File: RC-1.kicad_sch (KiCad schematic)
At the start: 0 parts

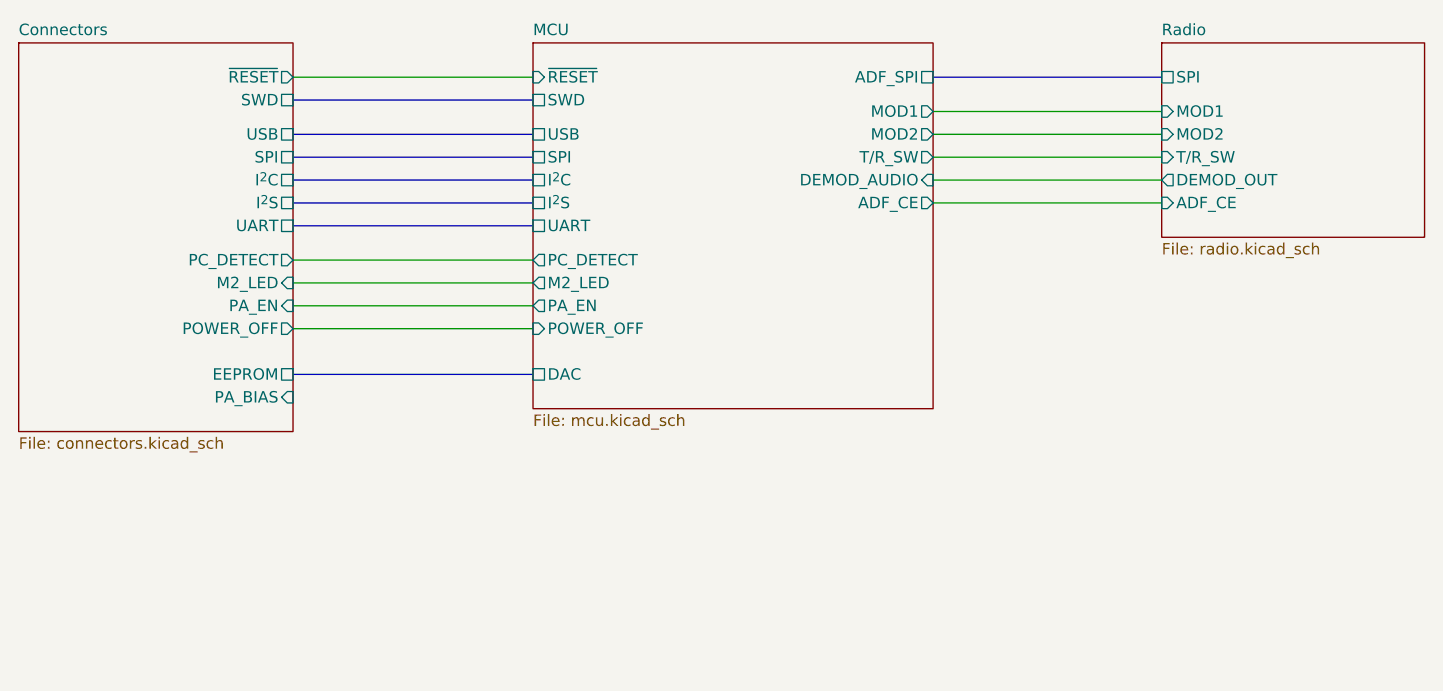
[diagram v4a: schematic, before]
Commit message: Set up ADF7021 for single RF output, 2-point modulation
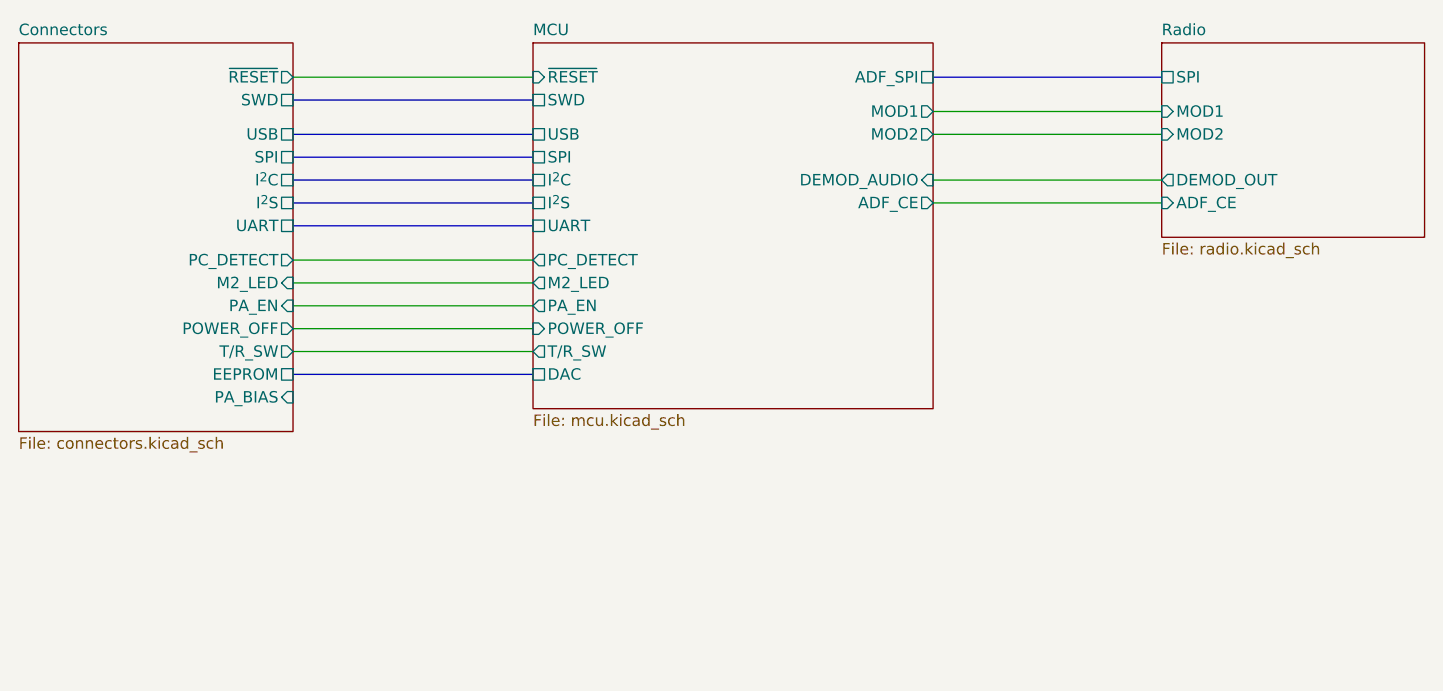
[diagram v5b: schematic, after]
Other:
- sheet Connectors ports: added T/R_SW; removed none
- sheet Radio ports: added none; removed T/R_SW
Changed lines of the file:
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@@
     (stroke (width 0) (type default) (color 0 0 0 0))
   )
-  (wire (pts (xy 175.26 93.98) (xy 200.66 93.98))
+  (wire (pts (xy 130.81 115.57) (xy 104.14 115.57))
     (stroke (width 0) (type default) (color 0 0 0 0))
   )
@@
       (effects (font (size 1.27 1.27)) (justify right))
     )
-    (pin "T{slash}R_SW" output (at 175.26 93.98 0)
-      (effects (font (size 1.27 1.27)) (justify right))
+    (pin "T{slash}R_SW" output (at 130.81 115.57 180)
+      (effects (font (size 1.27 1.27)) (justify left))
     )
     (pin "DEMOD_AUDIO" input (at 175.26 96.52 0)
@@
       (effects (font (size 1.27 1.27)) (justify right))
     )
+    (pin "T{slash}R_SW" output (at 104.14 115.57 0)
+      (effects (font (size 1.27 1.27)) (justify right))
+    )
   )
   (sheet (at 200.66 81.28) (size 29.21 21.59) (fields_autoplaced)
@@
       (effects (font (size 1.27 1.27)) (justify left top))
     )
-    (pin "T{slash}R_SW" input (at 200.66 93.98 180)
-      (effects (font (size 1.27 1.27)) (justify left))
-    )
     (pin "MOD2" input (at 200.66 91.44 180)
       (effects (font (size 1.27 1.27)) (justify left))
@@
       (reference "#PWR?") (unit 1) (value "+3V3") (footprint "")
     )
+    (path "/e9b5eb9e-a5da-44ea-89cf-1dbc5f8707b1/1950a0c7-f402-4b5c-a508-849658a6f4d3"
+      (reference "#PWR?") (unit 1) (value "GND") (footprint "")
+    )
     (path "/e9b5eb9e-a5da-44ea-89cf-1dbc5f8707b1/1b350a9d-a408-4dfa-a32b-dc704a4a856d"
       (reference "#PWR?") (unit 1) (value "GND") (footprint "")
@@
       (reference "#PWR?") (unit 1) (value "GND") (footprint "")
     )
+    (path "/e9b5eb9e-a5da-44ea-89cf-1dbc5f8707b1/2c4a4823-3df4-4715-82e4-ace04f59e52b"
+      (reference "#PWR?") (unit 1) (value "GND") (footprint "")
+    )
     (path "/e9b5eb9e-a5da-44ea-89cf-1dbc5f8707b1/321442de-1be8-447c-864f-6a257a7c6538"
       (reference "#PWR?") (unit 1) (value "GND") (footprint "")
@@
     )
     (path "/e9b5eb9e-a5da-44ea-89cf-1dbc5f8707b1/48b252b8-2440-494d-9928-f82258d5af1c"
+      (reference "#PWR?") (unit 1) (value "GND") (footprint "")
+    )
+    (path "/e9b5eb9e-a5da-44ea-89cf-1dbc5f8707b1/4d8c1cd9-f911-4b73-9309-ada4c43200a2"
       (reference "#PWR?") (unit 1) (value "GND") (footprint "")
     )
@@
       (reference "#PWR?") (unit 1) (value "GND") (footprint "")
     )
+    (path "/e9b5eb9e-a5da-44ea-89cf-1dbc5f8707b1/56056a77-a219-4861-a216-23f1af2f53ef"
+      (reference "#PWR?") (unit 1) (value "+3V3") (footprint "")
+    )
     (path "/37f64190-0af6-4571-a391-bfca4fb830ce/5a9912a7-bc78-4975-becd-a93d7e6ca124"
       (reference "#PWR?") (unit 1) (value "+3V3") (footprint "")
@@
     )
     (path "/e9b5eb9e-a5da-44ea-89cf-1dbc5f8707b1/857e3f02-6033-4b41-84a2-b44b517994ba"
+      (reference "#PWR?") (unit 1) (value "GND") (footprint "")
+    )
+    (path "/e9b5eb9e-a5da-44ea-89cf-1dbc5f8707b1/88e64f20-39b1-43e3-bc15-63ee762477d0"
       (reference "#PWR?") (unit 1) (value "GND") (footprint "")
     )
@@
       (reference "#PWR?") (unit 1) (value "+3V3") (footprint "")
     )
+    (path "/e9b5eb9e-a5da-44ea-89cf-1dbc5f8707b1/b49bf0fd-c72b-4a40-94e9-b96d52cc906a"
+      (reference "#PWR?") (unit 1) (value "GND") (footprint "")
+    )
     (path "/37f64190-0af6-4571-a391-bfca4fb830ce/be7cb700-3d99-4cd8-9ce6-aeefb1daeab8"
       (reference "#PWR?") (unit 1) (value "+3V3") (footprint "")
@@
       (reference "#PWR?") (unit 1) (value "+3V3") (footprint "")
     )
+    (path "/e9b5eb9e-a5da-44ea-89cf-1dbc5f8707b1/d0db605f-f64d-4084-99f0-1f083aec5dda"
+      (reference "#PWR?") (unit 1) (value "GND") (footprint "")
+    )
     (path "/d054b6a0-3a84-4aaa-901c-78f33fd51c3e/d8415da7-949b-463f-944b-f60c21219035"
       (reference "#PWR?") (unit 1) (value "GND") (footprint "")
@@
     (path "/37f64190-0af6-4571-a391-bfca4fb830ce/fa5153d6-bd2e-481c-acf5-a582605af947"
       (reference "#PWR?") (unit 1) (value "GND") (footprint "")
+    )
+    (path "/e9b5eb9e-a5da-44ea-89cf-1dbc5f8707b1/0101861e-4de8-4162-b9fa-983060e95190"
+      (reference "C?") (unit 1) (value "6p8") (footprint "Capacitor_SMD:C_0402_1005Metric")
     )
     (path "/37f64190-0af6-4571-a391-bfca4fb830ce/018002e6-06ae-46c7-887f-c27f45825467"
@@
       (reference "C?") (unit 1) (value "100n") (footprint "Capacitor_SMD:C_0402_1005Metric")
     )
+    (path "/e9b5eb9e-a5da-44ea-89cf-1dbc5f8707b1/69082dc9-e612-439f-b4a5-50360abc5713"
+      (reference "C?") (unit 1) (value "1n5") (footprint "Capacitor_SMD:C_0603_1608Metric")
+    )
     (path "/e9b5eb9e-a5da-44ea-89cf-1dbc5f8707b1/6c002c11-1dba-4213-acac-eaa28178d048"
       (reference "C?") (unit 1) (value "6p8") (footprint "Capacitor_SMD:C_0402_1005Metric")
@@
       (reference "C?") (unit 1) (value "10n") (footprint "Capacitor_SMD:C_0402_1005Metric")
     )
+    (path "/e9b5eb9e-a5da-44ea-89cf-1dbc5f8707b1/777b7d5e-dac0-4871-a578-c644ad7014c7"
+      (reference "C?") (unit 1) (value "1n5") (footprint "Capacitor_SMD:C_0603_1608Metric")
+    )
+    (path "/e9b5eb9e-a5da-44ea-89cf-1dbc5f8707b1/92b7986c-f593-49ae-8d36-f50fcd9da6e2"
+      (reference "C?") (unit 1) (value "1n5") (footprint "Capacitor_SMD:C_0603_1608Metric")
+    )
+    (path "/e9b5eb9e-a5da-44ea-89cf-1dbc5f8707b1/a03ac130-fa79-40b1-a286-2b47aff1a3e5"
+      (reference "C?") (unit 1) (value "10n") (footprint "Capacitor_SMD:C_0402_1005Metric")
+    )
     (path "/37f64190-0af6-4571-a391-bfca4fb830ce/a3ee2e41-11fd-443f-86c5-416e10b6f0a0"
       (reference "C?") (unit 1) (value "100n") (footprint "Capacitor_SMD:C_0402_1005Metric")
@@
       (reference "C?") (unit 1) (value "100n") (footprint "Capacitor_SMD:C_0402_1005Metric")
     )
+    (path "/e9b5eb9e-a5da-44ea-89cf-1dbc5f8707b1/d4e5561e-4a4e-484b-ad69-8cb687deefc3"
+      (reference "C?") (unit 1) (value "220p") (footprint "Capacitor_SMD:C_0402_1005Metric")
+    )
     (path "/37f64190-0af6-4571-a391-bfca4fb830ce/dbc23c1d-f9c7-4c2e-b8da-96344fb20002"
       (reference "C?") (unit 1) (value "TBD") (footprint "Capacitor_SMD:C_0402_1005Metric")
@@
       (reference "J?") (unit 1) (value "U.FL") (footprint "Connector_Coaxial:U.FL_Hirose_U.FL-R-SMT-1_Vertical")
     )
+    (path "/e9b5eb9e-a5da-44ea-89cf-1dbc5f8707b1/428c4882-4fa2-4105-96dc-a3e7f24d9294"
+      (reference "L?") (unit 1) (value "20n") (footprint "Inductor_SMD:L_0603_1608Metric")
+    )
     (path "/e9b5eb9e-a5da-44ea-89cf-1dbc5f8707b1/8d7ae6cb-fe9e-418c-b7a9-b5bf2fb70c94"
       (reference "L?") (unit 1) (value "27n") (footprint "Inductor_SMD:L_0402_1005Metric")
     )
+    (path "/e9b5eb9e-a5da-44ea-89cf-1dbc5f8707b1/978703e1-c453-44f6-8424-3709a0ab4260"
+      (reference "L?") (unit 1) (value "22n") (footprint "Inductor_SMD:L_0603_1608Metric")
+    )
     (path "/37f64190-0af6-4571-a391-bfca4fb830ce/bdf5539d-1394-4ecb-ae85-1bb323c82721"
       (reference "L?") (unit 1) (value "10uH") (footprint "")
     )
+    (path "/e9b5eb9e-a5da-44ea-89cf-1dbc5f8707b1/d72d702d-497f-4bad-82eb-724930a27ad6"
+      (reference "L?") (unit 1) (value "13n") (footprint "Inductor_SMD:L_0402_1005Metric")
+    )
     (path "/e9b5eb9e-a5da-44ea-89cf-1dbc5f8707b1/e850d9e7-ba6d-4b13-88a3-4477f9540cd9"
       (reference "L?") (unit 1) (value "DNP") (footprint "Inductor_SMD:L_0603_1608Metric")
@@
       (reference "R?") (unit 1) (value "100k") (footprint "Resistor_SMD:R_0402_1005Metric")
     )
+    (path "/e9b5eb9e-a5da-44ea-89cf-1dbc5f8707b1/547c7d2e-dd6a-4751-bc89-ad162b03611c"
+      (reference "R?") (unit 1) (value "5k6") (footprint "Resistor_SMD:R_0603_1608Metric")
+    )
     (path "/37f64190-0af6-4571-a391-bfca4fb830ce/57824045-fda2-4d7c-9a10-82e8e242782c"
       (reference "R?") (unit 1) (value "4k7") (footprint "")
@@
       (reference "R?") (unit 1) (value "4k7") (footprint "")
     )
+    (path "/e9b5eb9e-a5da-44ea-89cf-1dbc5f8707b1/7214f97a-296e-4985-b4fa-b4ba473d6345"
+      (reference "R?") (unit 1) (value "5k6") (footprint "Resistor_SMD:R_0603_1608Metric")
+    )
     (path "/e9b5eb9e-a5da-44ea-89cf-1dbc5f8707b1/76c55351-7a65-4876-8a89-0c66ad3aba52"
       (reference "R?") (unit 1) (value "47k") (footprint "Resistor_SMD:R_0402_1005Metric")
@@
       (reference "R?") (unit 1) (value "3r9") (footprint "Resistor_SMD:R_0402_1005Metric")
     )
+    (path "/e9b5eb9e-a5da-44ea-89cf-1dbc5f8707b1/dbe8e1c9-882e-4adc-b8a0-b190bbaac178"
+      (reference "R?") (unit 1) (value "5k6") (footprint "Resistor_SMD:R_0603_1608Metric")
+    )
     (path "/e9b5eb9e-a5da-44ea-89cf-1dbc5f8707b1/df0e692a-a3e9-49b8-952e-049ef2825c87"
       (reference "R?") (unit 1) (value "22k") (footprint "Resistor_SMD:R_0402_1005Metric")
@@
       (reference "R?") (unit 1) (value "10k") (footprint "Resistor_SMD:R_0402_1005Metric")
     )
+    (path "/e9b5eb9e-a5da-44ea-89cf-1dbc5f8707b1/562e70e0-8e6c-4391-ae4b-5af8b375bd80"
+      (reference "TP?") (unit 1) (value "TestPoint_Probe") (footprint "TestPoint:TestPoint_Pad_D1.0mm")
+    )
     (path "/e9b5eb9e-a5da-44ea-89cf-1dbc5f8707b1/7111717d-b5c1-4f07-ba9a-64a0e2194759"
       (reference "TP?") (unit 1) (value "TestPoint_Probe") (footprint "")
     )
+    (path "/e9b5eb9e-a5da-44ea-89cf-1dbc5f8707b1/8693ee46-df55-4bdc-9879-b00208ba659b"
+      (reference "TP?") (unit 1) (value "TestPoint_Probe") (footprint "TestPoint:TestPoint_Pad_D1.0mm")
+    )
     (path "/e9b5eb9e-a5da-44ea-89cf-1dbc5f8707b1/a0a55d21-4d59-45bb-bff9-83fb9f5419c2"
